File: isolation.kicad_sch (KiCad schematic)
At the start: 39 parts, among them J2 NAPPE_FILAMENT_HT, U1 UCC27517, U12 UCC24612, U13 SN74LVC1G08, U3 ISO7710, U5 DPC817, U7 AMC0311R, U8 AMC0311R, U9 AMC0302R

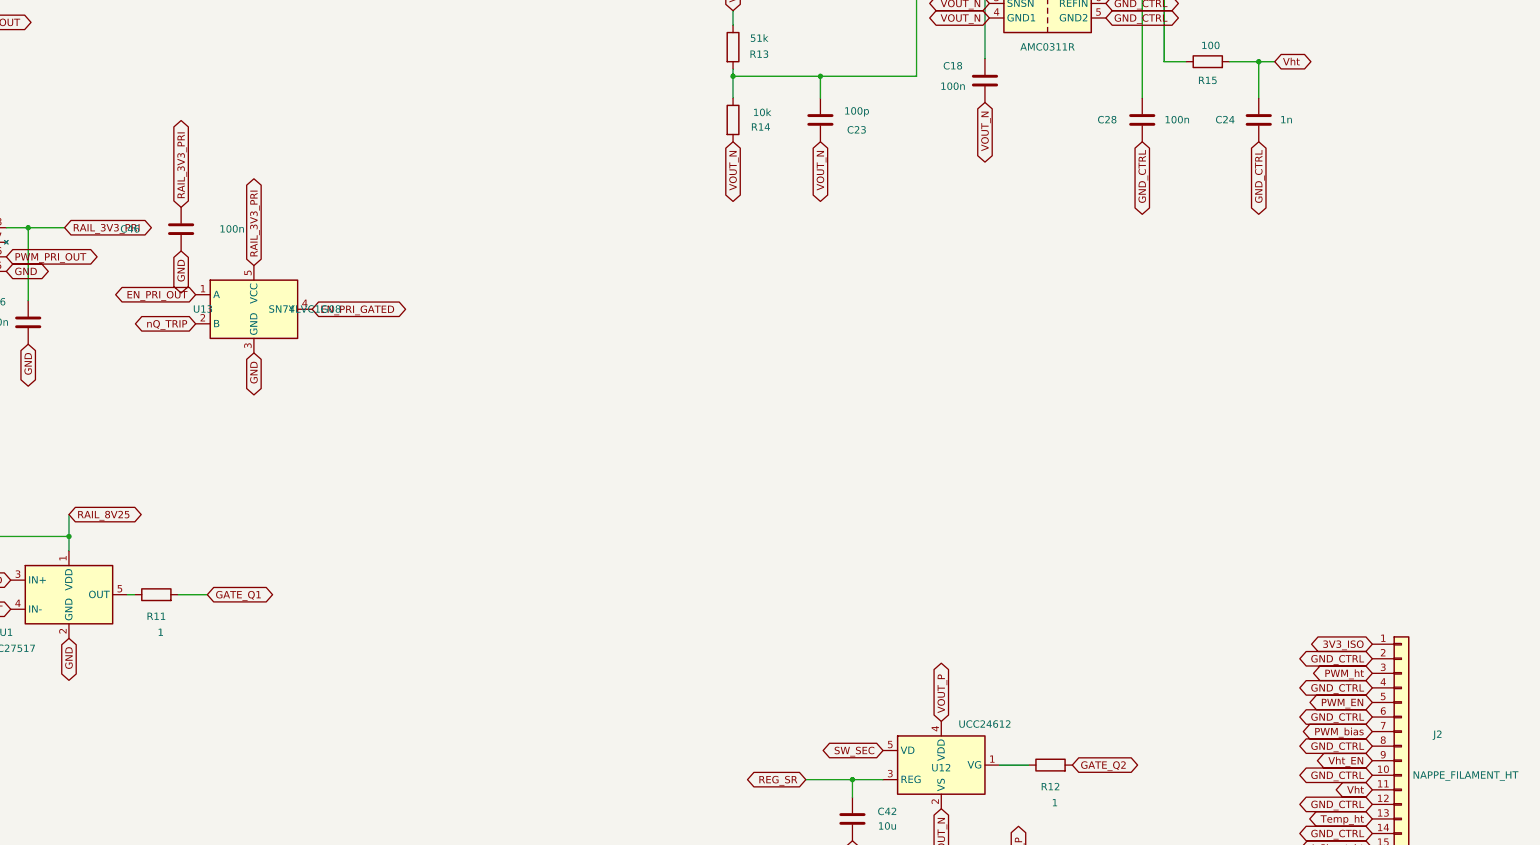
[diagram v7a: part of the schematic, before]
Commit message: Ajoute une LED de defaut sur Q_TRIP (R34/D6), corrige un bug d'insertion lib_symbols
Q_TRIP (sortie de reserve du verrou) recoit un usage reel : LED rouge 3mm
+ 10k, polarite ajustee par l'utilisateur pour s'allumer en defaut latche
(Q_TRIP -> D6 -> R34 -> GND, verifie par export netlist).

Corrige au passage une insertion incorrecte du bloc lib_symbols de
Device:LED (imbrique par erreur dans l'etiquette globale ISNS_AMP au lieu
de suivre la vraie fermeture de lib_symbols), qui empechait le chargement
de la feuille. Documente dans l'addendum du S19.

Co-Authored-By: Claude Sonnet 5 <noreply@anthropic.com>
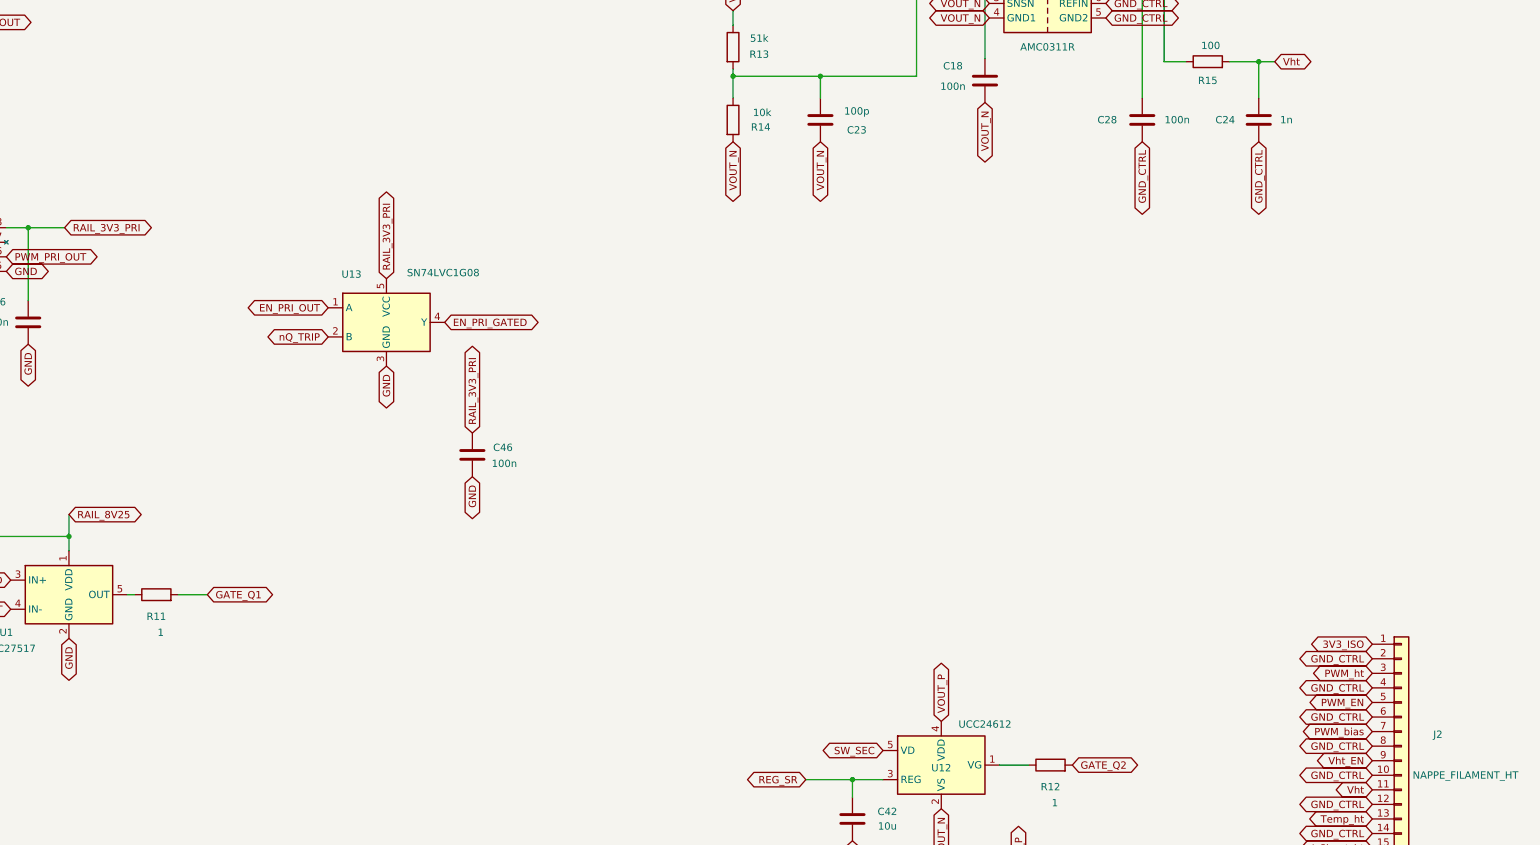
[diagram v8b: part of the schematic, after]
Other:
- moved on the sheet: C46, U13
